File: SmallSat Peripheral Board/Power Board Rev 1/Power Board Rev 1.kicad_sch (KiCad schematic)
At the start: 39 parts, among them J1 Conn_01x02_Pin, J2 Conn_01x02_Pin, U1 DMN3020UFDF, U2 BQ296202DSGR, U3 DMN3020UFDF, U4 BQ28Z620DRZR, U5 TPS62993QRYTRQ1, U6 TPS62993QRYTRQ1

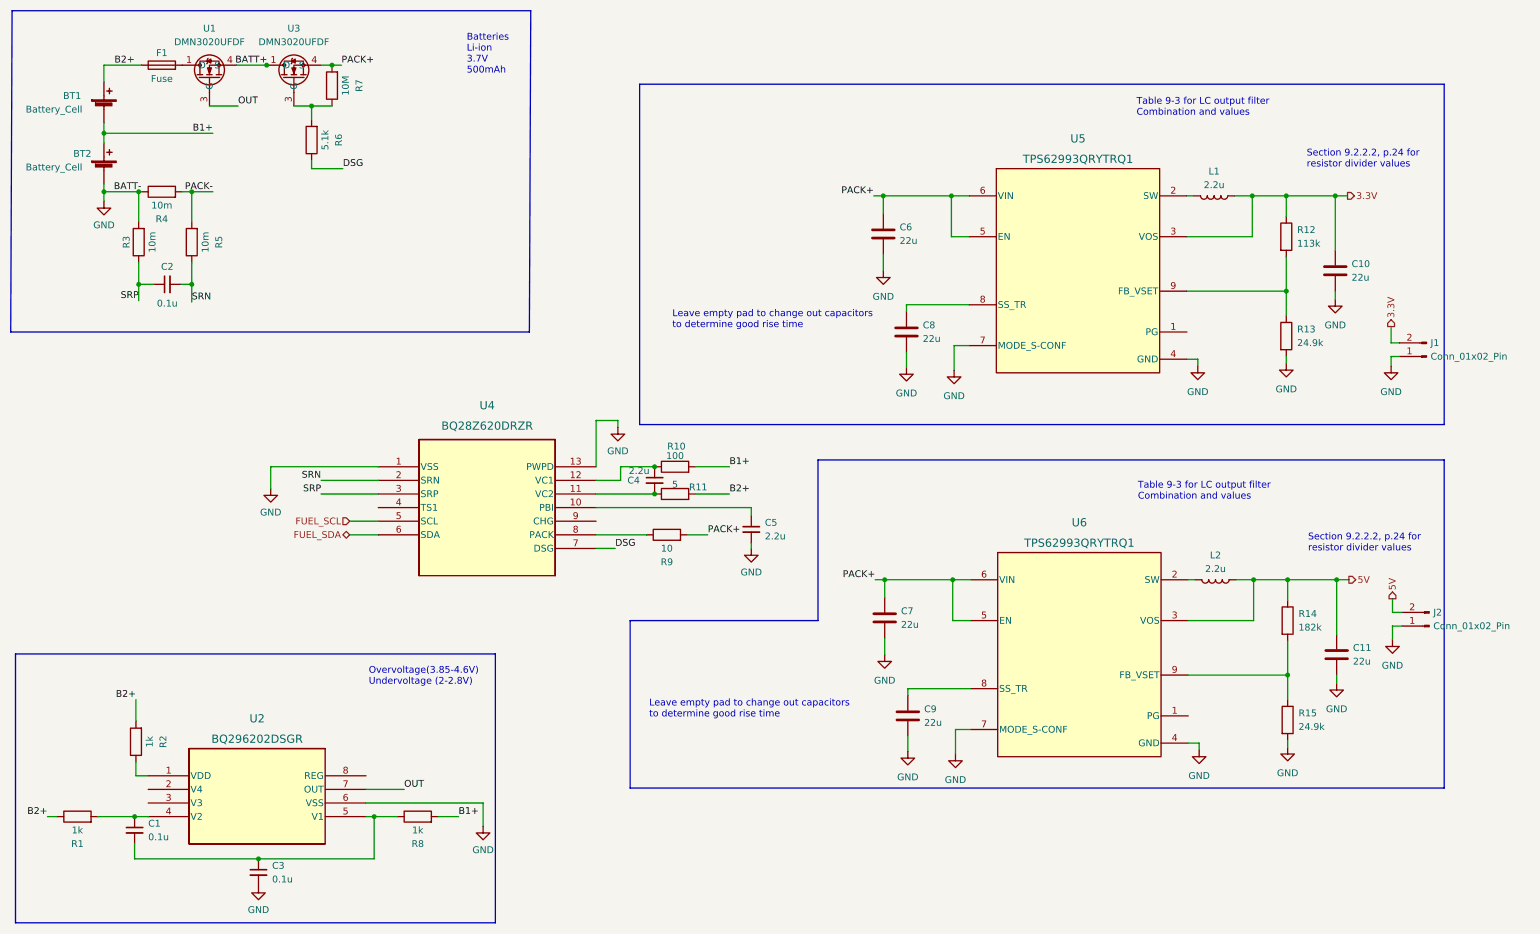
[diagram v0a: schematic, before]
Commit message: Power Board Grouping
- Continuing to group parts
- Connectors figured out
- Filter circuit must be close to BQ298
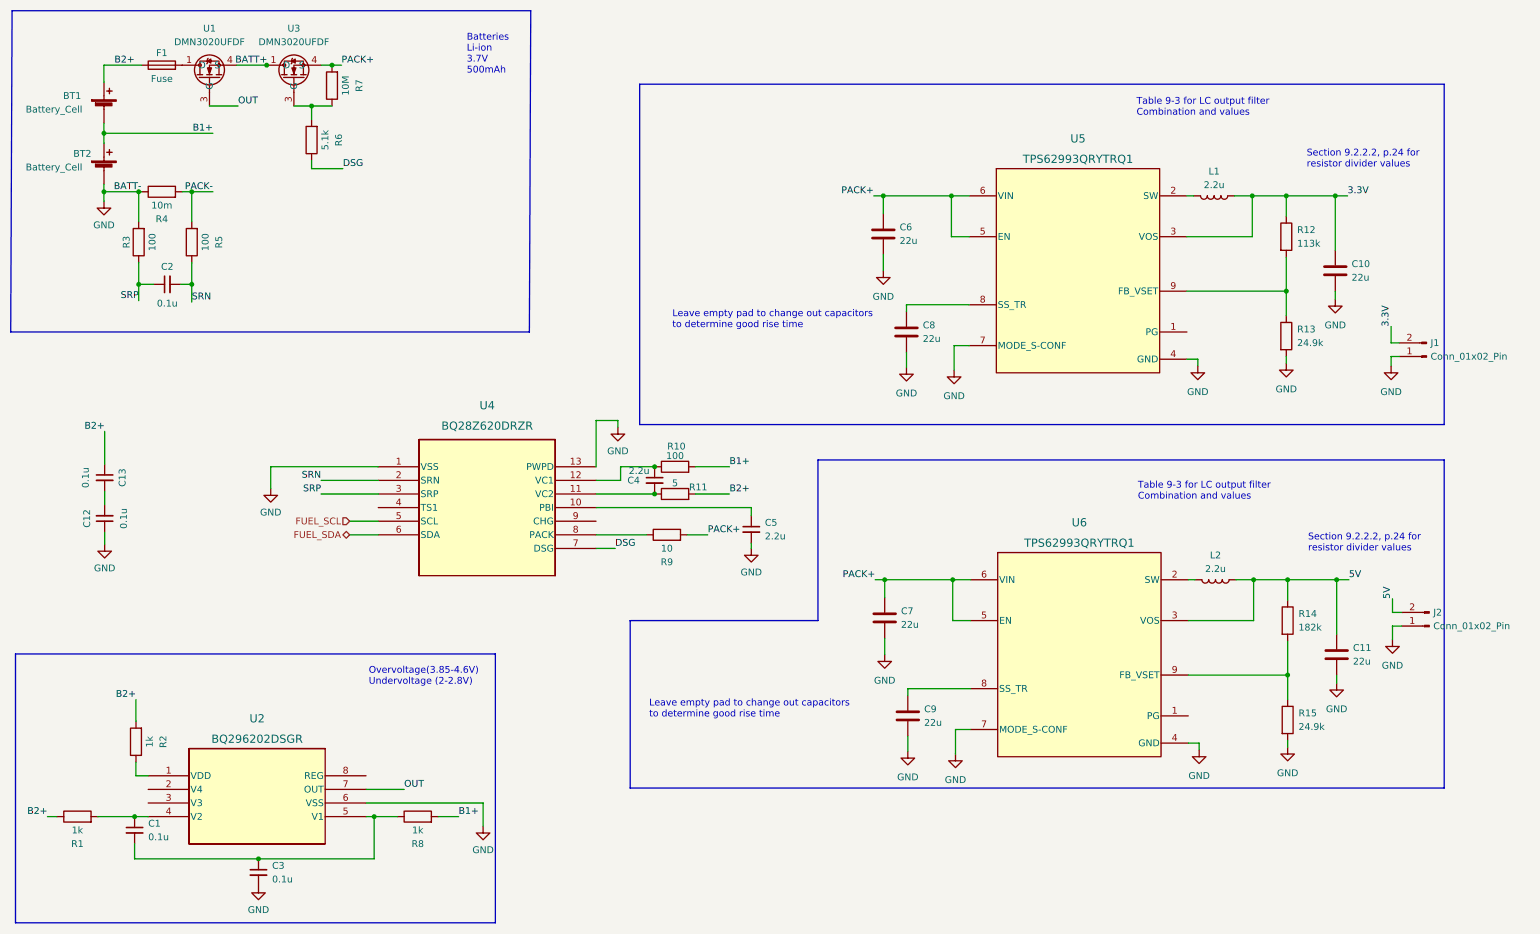
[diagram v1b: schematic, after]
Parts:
- added C12, C13: 0.1u, Capacitor_SMD:C_1206_3216Metric, symbol Device:C_Small
- J1, J2: footprint (none) -> Connector_PinSocket_1.00mm:PinSocket_1x02_P1.00mm_Vertical
- L1, L2: footprint Capacitor_SMD:C_1206_3216Metric -> Inductor_SMD:L_1206_3216Metric
- R3, R5: value 10m -> 100
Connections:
- net B2+: now also C13.1
- net GND: now also C12.1
- new net: C12.2, C13.2
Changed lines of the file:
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@@
+    (stroke (width 0) (type default))
+  )
+  (wire (pts (xy 33.274 95.758) (xy 33.274 101.854))
     (stroke (width 0) (type default))
   )
@@
     (stroke (width 0) (type default))
   )
+  (wire (pts (xy 33.274 114.554) (xy 33.274 116.84))
+    (stroke (width 0) (type default))
+  )
   (wire (pts (xy 38.862 172.72) (xy 38.862 175.514))
     (stroke (width 0) (type default))
@@
   )
   (wire (pts (xy 273.558 129.54) (xy 273.558 127))
+    (stroke (width 0) (type default))
+  )
+  (wire (pts (xy 33.274 106.934) (xy 33.274 109.474))
     (stroke (width 0) (type default))
   )
@@
     (effects (font (size 1.27 1.27)) (justify right bottom))
   )
+  (label "3.3V" (at 265.176 51.816 0) (fields_autoplaced)
+    (effects (font (size 1.27 1.27)) (justify left bottom))
+  )
   (label "B1+" (at 99.314 167.64 0) (fields_autoplaced)
     (effects (font (size 1.27 1.27)) (justify left bottom))
@@
     (effects (font (size 1.27 1.27)) (justify right bottom))
   )
+  (label "5V" (at 265.43 123.444 0) (fields_autoplaced)
+    (effects (font (size 1.27 1.27)) (justify left bottom))
+  )
   (label "PACK+" (at 145.796 115.062 0) (fields_autoplaced)
     (effects (font (size 1.27 1.27)) (justify left bottom))
+  )
+  (label "B2+" (at 33.274 95.758 180) (fields_autoplaced)
+    (effects (font (size 1.27 1.27)) (justify right bottom))
   )
   (label "B2+" (at 38.862 27.432 180) (fields_autoplaced)
@@
     (effects (font (size 1.27 1.27)) (justify left bottom))
   )
+  (label "3.3V" (at 273.304 76.2 90) (fields_autoplaced)
+    (effects (font (size 1.27 1.27)) (justify left bottom))
+  )
+  (label "5V" (at 273.558 127 90) (fields_autoplaced)
+    (effects (font (size 1.27 1.27)) (justify left bottom))
+  )
   (label "BATT-" (at 40.132 51.054 180) (fields_autoplaced)
     (effects (font (size 1.27 1.27)) (justify right bottom))
@@
     (effects (font (size 1.27 1.27)) (justify right bottom))
   )
-  (hierarchical_label "5V" (shape output) (at 273.558 127 90) (fields_autoplaced)
-    (effects (font (size 1.27 1.27)) (justify left))
-  )
-  (hierarchical_label "3.3V" (shape output) (at 265.176 51.816 0) (fields_autoplaced)
-    (effects (font (size 1.27 1.27)) (justify left))
-  )
-  (hierarchical_label "5V" (shape output) (at 265.43 123.444 0) (fields_autoplaced)
-    (effects (font (size 1.27 1.27)) (justify left))
-  )
   (hierarchical_label "FUEL_SCL" (shape input) (at 78.994 112.522 180) (fields_autoplaced)
     (effects (font (size 1.27 1.27)) (justify right))
-  )
-  (hierarchical_label "3.3V" (shape output) (at 273.304 76.2 90) (fields_autoplaced)
-    (effects (font (size 1.27 1.27)) (justify left))
   )
   (hierarchical_label "FUEL_SDA" (shape bidirectional) (at 78.994 115.062 180) (fields_autoplaced)
@@
       (effects (font (size 1.27 1.27)))
     )
-    (property "Value" "10m" (at 42.164 60.452 90)
+    (property "Value" "100" (at 42.164 60.452 90)
       (effects (font (size 1.27 1.27)))
     )
@@
     )
   )
+  (symbol (lib_id "Device:C_Small") (at 33.274 104.394 0) (unit 1)
+    (in_bom yes) (on_board yes) (dnp no)
+    (property "Reference" "C13" (at 36.576 104.394 90)
+      (effects (font (size 1.27 1.27)))
+    )
+    (property "Value" "0.1u" (at 29.718 104.394 90)
+      (effects (font (size 1.27 1.27)))
+    )
+    (property "Footprint" "Capacitor_SMD:C_1206_3216Metric" (at 33.274 104.394 0)
+      (effects (font (size 1.27 1.27)) hide)
+    )
+    (property "Datasheet" "~" (at 33.274 104.394 0)
+      (effects (font (size 1.27 1.27)) hide)
+    )
+    (pin "1")
+    (pin "2")
+    (instances
+      (project "Power Board Rev 1"
+        (path "/150b62dd-248a-437a-aec7-a71760bbbd98"
+          (reference "C13") (unit 1)
+        )
+      )
+    )
+  )
   (symbol (lib_id "power:GND") (at 182.88 83.82 0) (unit 1)
     (in_bom yes) (on_board yes) (dnp no) (fields_autoplaced)
@@
       (effects (font (size 1.27 1.27)))
     )
-    (property "Value" "5" (at 139.7 105.664 90)
+    (property "Value" "5" (at 139.7 105.41 90)
       (effects (font (size 1.27 1.27)))
     )
@@
       (effects (font (size 1.27 1.27)))
     )
-    (property "Value" "10m" (at 52.07 60.452 90)
+    (property "Value" "100" (at 52.07 60.452 90)
       (effects (font (size 1.27 1.27)))
     )
@@
       (effects (font (size 1.27 1.27)) (justify right))
     )
-    (property "Footprint" "" (at 279.908 81.788 0)
+    (property "Footprint" "Connector_PinSocket_1.00mm:PinSocket_1x02_P1.00mm_Vertical" (at 279.908 81.788 0)
       (effects (font (size 1.27 1.27)) hide)
     )
@@
       (effects (font (size 1.27 1.27)))
     )
-    (property "Footprint" "Capacitor_SMD:C_1206_3216Metric" (at 240.284 51.816 0)
+    (property "Footprint" "Inductor_SMD:L_1206_3216Metric" (at 240.284 51.816 0)
       (effects (font (size 1.27 1.27)) hide)
     )
@@
         (path "/150b62dd-248a-437a-aec7-a71760bbbd98"
           (reference "#PWR015") (unit 1)
+        )
+      )
+    )
+  )
+  (symbol (lib_id "power:GND") (at 33.274 116.84 0) (unit 1)
+    (in_bom yes) (on_board yes) (dnp no) (fields_autoplaced)
+    (property "Reference" "#PWR021" (at 33.274 123.19 0)
+      (effects (font (size 1.27 1.27)) hide)
+    )
+    (property "Value" "GND" (at 33.274 121.285 0)
+      (effects (font (size 1.27 1.27)))
+    )
+    (property "Footprint" "" (at 33.274 116.84 0)
+      (effects (font (size 1.27 1.27)) hide)
+    )
+    (property "Datasheet" "" (at 33.274 116.84 0)
+      (effects (font (size 1.27 1.27)) hide)
+    )
+    (pin "1")
+    (instances
+      (project "Power Board Rev 1"
+        (path "/150b62dd-248a-437a-aec7-a71760bbbd98"
+          (reference "#PWR021") (unit 1)
         )
       )
@@
       (effects (font (size 1.27 1.27)) (justify right))
     )
-    (property "Footprint" "" (at 280.416 132.08 0)
+    (property "Footprint" "Connector_PinSocket_1.00mm:PinSocket_1x02_P1.00mm_Vertical" (at 280.416 132.08 0)
       (effects (font (size 1.27 1.27)) hide)
     )
@@
       (effects (font (size 1.27 1.27)))
     )
-    (property "Footprint" "Capacitor_SMD:C_1206_3216Metric" (at 240.538 123.444 0)
+    (property "Footprint" "Inductor_SMD:L_1206_3216Metric" (at 240.538 123.444 0)
       (effects (font (size 1.27 1.27)) hide)
     )
@@
         )
       )
+    )
+  )
+  (symbol (lib_id "Device:C_Small") (at 33.274 112.014 180) (unit 1)
+    (in_bom yes) (on_board yes) (dnp no)
+    (property "Reference" "C12" (at 29.972 112.014 90)
+      (effects (font (size 1.27 1.27)))
+    )
+    (property "Value" "0.1u" (at 36.83 112.014 90)
+      (effects (font (size 1.27 1.27)))
+    )
+    (property "Footprint" "Capacitor_SMD:C_1206_3216Metric" (at 33.274 112.014 0)
+      (effects (font (size 1.27 1.27)) hide)
+    )
+    (property "Datasheet" "~" (at 33.274 112.014 0)
+      (effects (font (size 1.27 1.27)) hide)
+    )
+    (pin "1")
+    (pin "2")
+    (instances
+      (project "Power Board Rev 1"
+        (path "/150b62dd-248a-437a-aec7-a71760bbbd98"
+          (reference "C12") (unit 1)
+        )
+      )

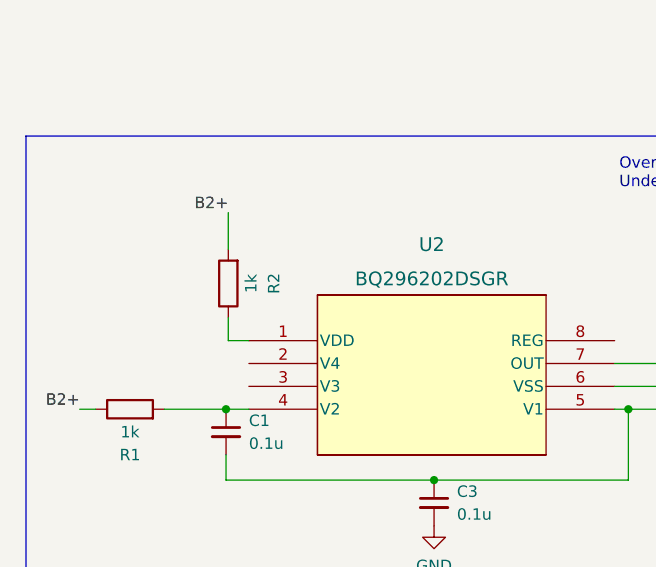
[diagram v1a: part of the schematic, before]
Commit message: Current Line Outline Complete
- OV/UV protection IC wired
- fuel gauge not wired
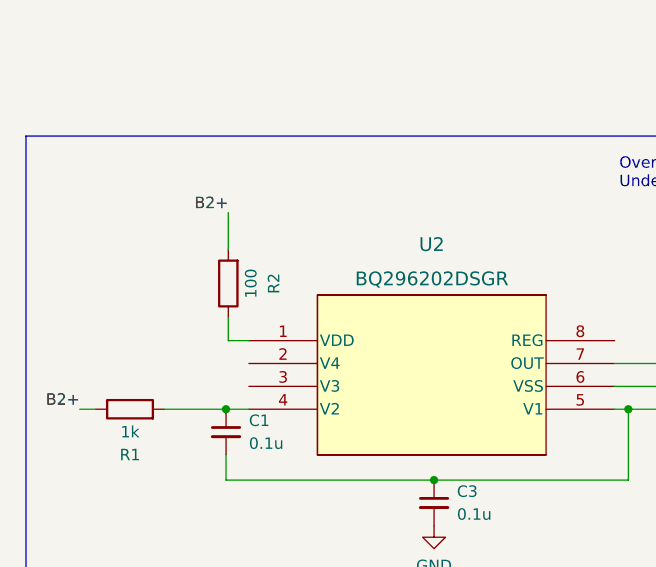
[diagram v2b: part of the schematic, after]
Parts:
- R2: value 1k -> 100
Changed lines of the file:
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@@
       (effects (font (size 1.27 1.27)))
     )
-    (property "Value" "1k" (at 41.656 153.67 90)
+    (property "Value" "100" (at 41.656 153.67 90)
       (effects (font (size 1.27 1.27)))
     )

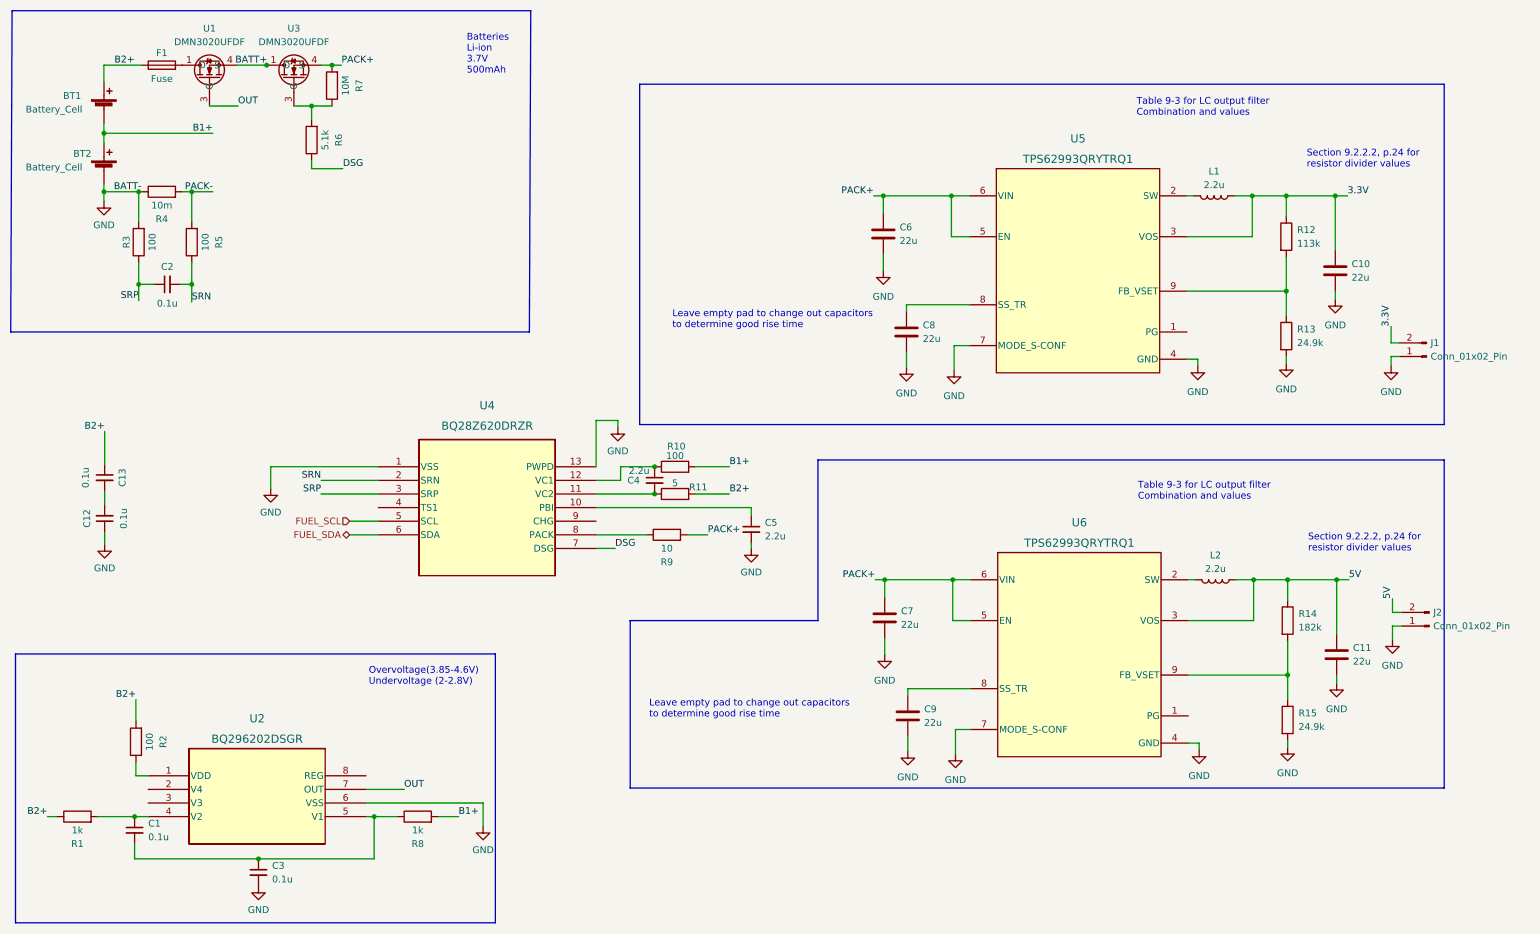
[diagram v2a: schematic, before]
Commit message: Power Board Connections Complete
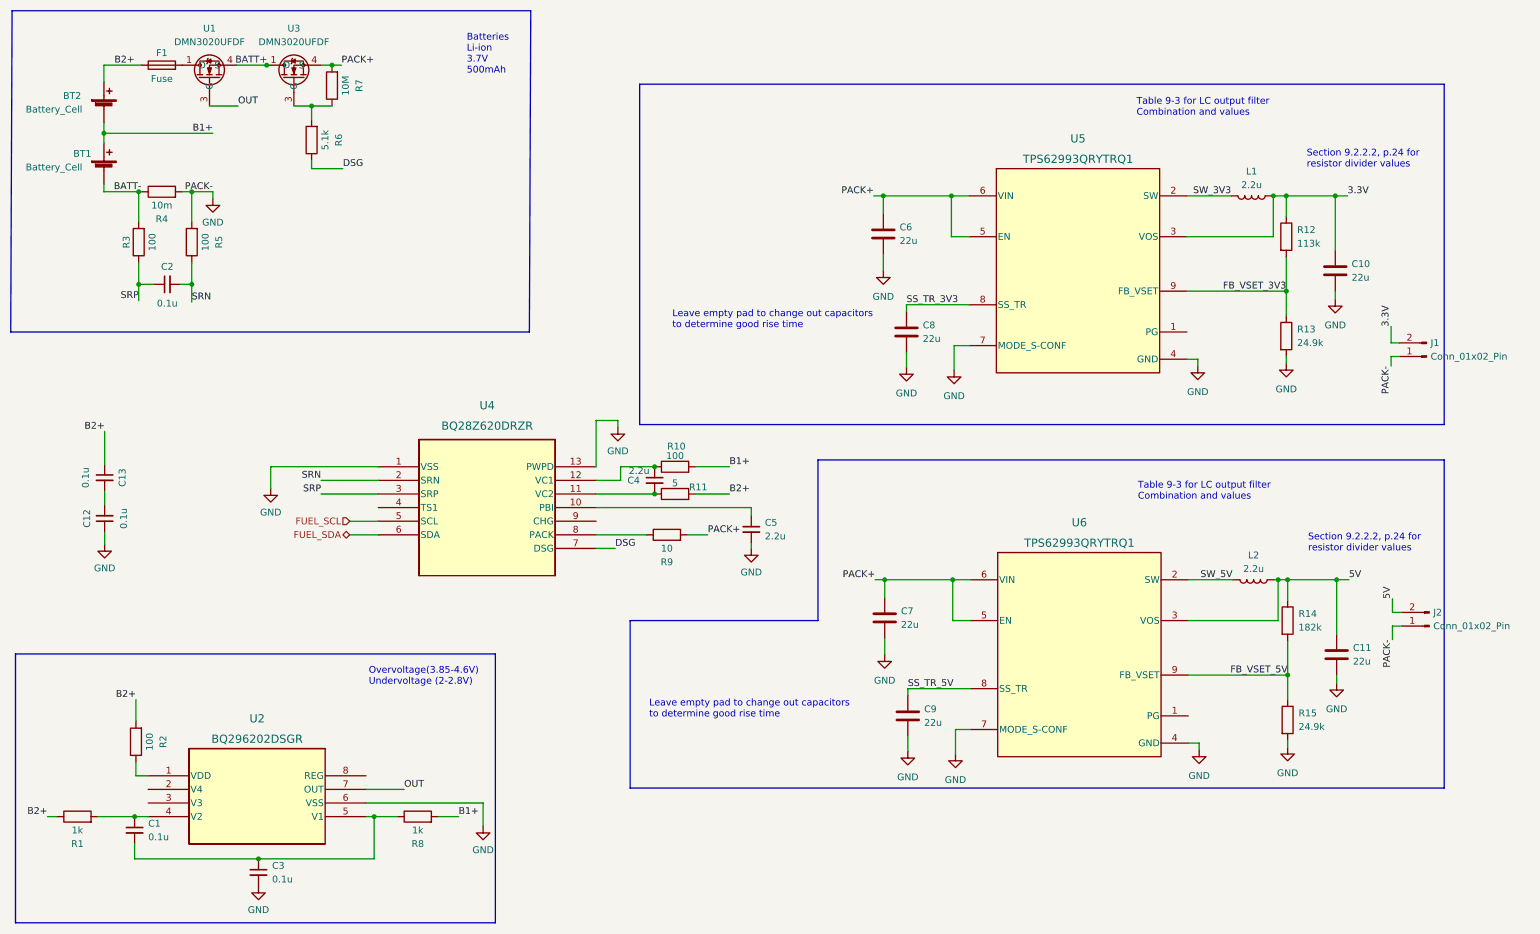
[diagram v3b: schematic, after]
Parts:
- C10, C11, C6, C7, C8, C9: footprint Capacitor_SMD:C_1206_3216Metric -> Capacitor_SMD:C_0402_1005Metric
- R12, R13, R14, R15: footprint Resistor_SMD:R_1206_3216Metric -> Resistor_SMD:R_0402_1005Metric
- renumbered BT2 to BT1, BT1 to BT2
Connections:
- net PACK- is gone; now on net GND: R4.2, R5.2
- net GND: no longer BT1.2 (-), R3.2, R4.1
- net SW_3V3: now reaches L1.2, U5.2 (SW)
- net SS_TR_3V3: now reaches C8.1, U5.8 (SS_TR)
- net FB_VSET_3V3: now reaches R12.2, R13.1, U5.9 (FB_VSET)
- net FB_VSET_5V: now reaches R14.2, R15.1, U6.9 (FB_VSET)
- net SW_5V: now reaches L2.2, U6.2 (SW)
- net SS_TR_5V: now reaches C9.1, U6.8 (SS_TR)
- new net BATT-: BT1.2 (-), R3.2, R4.1
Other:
- moved on the sheet: L1, L2
